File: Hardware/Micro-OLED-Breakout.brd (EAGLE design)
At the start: 27.9 x 21.6 mm, 23 parts

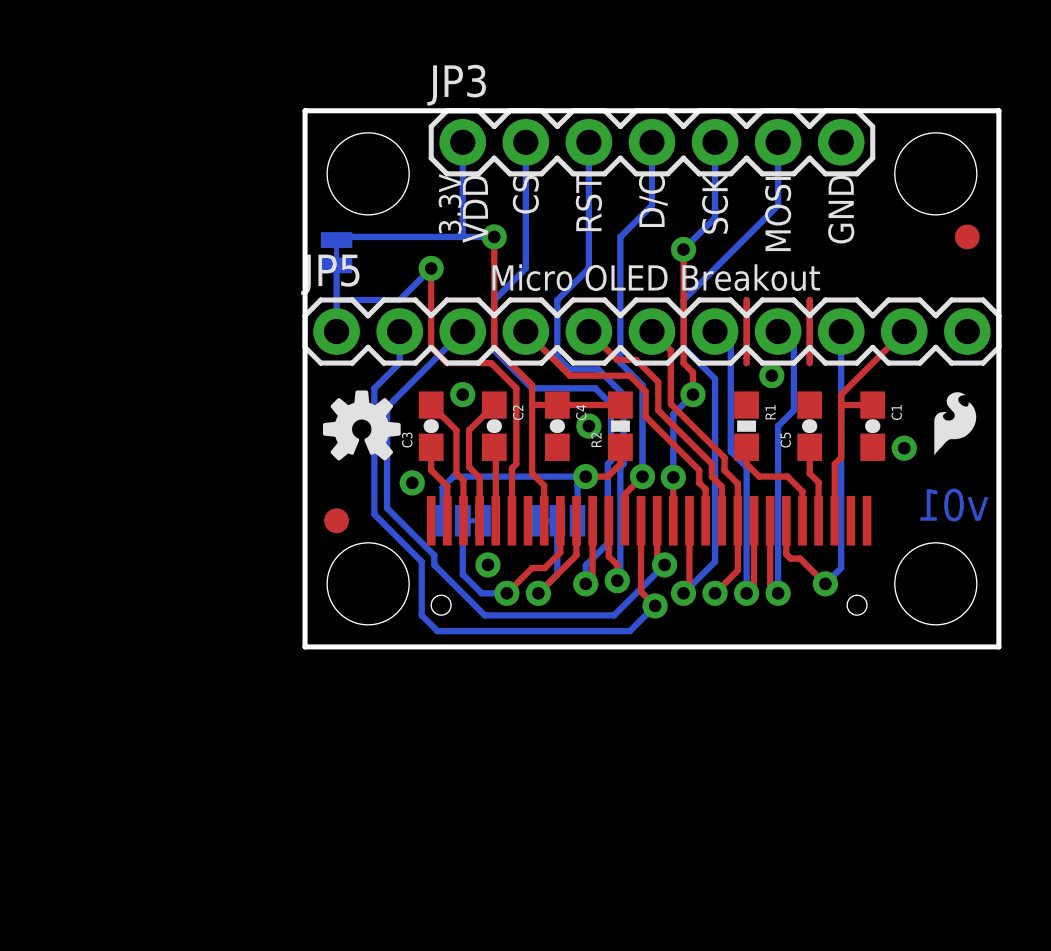
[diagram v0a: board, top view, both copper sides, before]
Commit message: Revising board shape, OLED (v02)
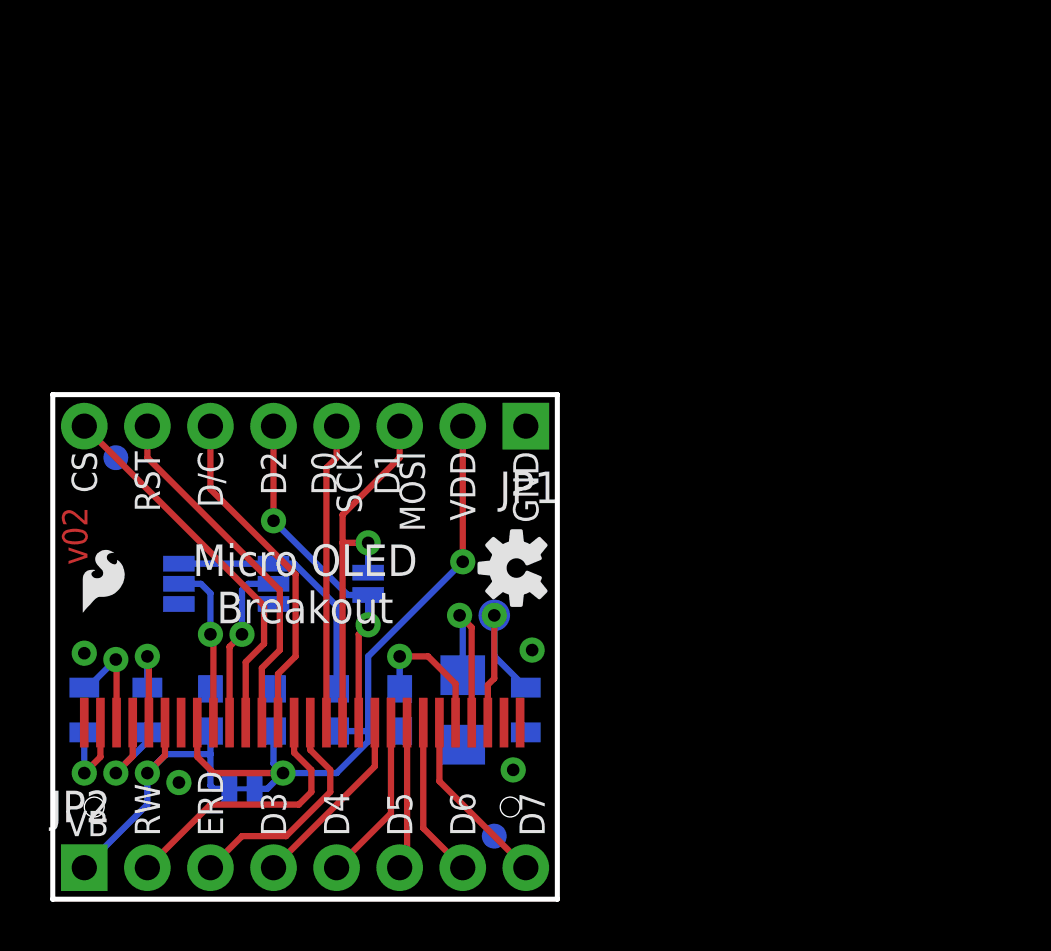
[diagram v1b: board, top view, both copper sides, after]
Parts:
- removed JP3: (no value), SparkFun-Connectors:1X07
- removed JP5: M11PTH, SparkFun-Connectors:1X11
- removed STANDOFF1, STANDOFF2, STANDOFF3, STANDOFF4: STAND-OFF, SparkFun-Electromechanical:STAND-OFF
- added C6: 1uF, SparkFun-Passives:0603-CAP
- added JP1, JP2: (no value), SparkFun-Connectors:1X08_PIN1_NO_SILK
- added LOGO4: SFE_LOGO_FLAME.1_INCH, SparkFun-Aesthetics:SFE_LOGO_FLAME_.1
- added SJ5: (no value), SparkFun-Passives:PAD-JUMPER-2-NO_YES_SILK
- added TP1: TEST-POINT3X5, SparkFun-Passives:PAD.03X.05
- C1: device SparkFun-Passives:0603-CAP -> SparkFun-Passives:0805
- C2: value 1uF 16V X5R -> 1uF X5R; device SparkFun-Passives:0603-CAP -> SparkFun-Passives:0805
- C3: value 1uF/16V X5R -> 1uF X5R; device SparkFun-Passives:0603-CAP -> SparkFun-Passives:0805
- C5: value 4.7uF/16V X7R -> 4.7uF/16V; device SparkFun-Passives:0603-CAP -> SparkFun-Passives:1206
- LOGO3: value SFE_LOGO_NAME_FLAME.1_INCH -> OSHW-LOGOS; device SparkFun-Aesthetics:SFE_LOGO_NAME_FLAME_.1 -> SparkFun-Aesthetics:OSHW-LOGO-S
- R2: value (none) -> 10k
- SJ1: value (none) -> BS1; device SparkFun-Passives:PAD-JUMPER-3-2OF3_NC_BY_TRACE_YES_SILK_FULL_BOX -> SparkFun-Passives:PAD-JUMPER-3-2OF3_NC_BY_PASTE_YES_SILK_FULL_BOX
- SJ2: value (none) -> BS2; device SparkFun-Passives:PAD-JUMPER-3-2OF3_NC_BY_TRACE_YES_SILK_FULL_BOX -> SparkFun-Passives:PAD-JUMPER-3-2OF3_NC_BY_PASTE_YES_SILK_FULL_BOX
- SJ3: device SparkFun-Passives:PAD-JUMPER-2-NC_BY_TRACE_YES_SILK -> SparkFun-Passives:PAD-JUMPER-2-NC_BY_TRACE_NO_SILK
- moved LOGO2 34.9 mm to (-9.27, 1.02)
- moved FID1 30.7 mm to (7.62, -7.62), flipped to the bottom
- moved SJ3 21.9 mm to (-2.54, -5.71), turned to 180 degrees
- moved C1 18.1 mm to (8.89, -2.54), flipped to the bottom
- moved C2 18.1 mm to (-6.35, -2.54), flipped to the bottom, turned to 90 degrees
- moved C3 18.1 mm to (-8.89, -2.54), flipped to the bottom
- moved C5 18.1 mm to (6.35, -2.54), flipped to the bottom, turned to 270 degrees
- moved R1 18.1 mm to (3.81, -2.54), flipped to the bottom, turned to 90 degrees
- moved FRAME1 16.3 mm to (-17.8, -19.1)
- moved C4 16.2 mm to (-1.27, -2.54), flipped to the bottom, turned to 90 degrees
- moved R2 16.2 mm to (1.27, -2.54), flipped to the bottom, turned to 270 degrees
- moved OLED1 16.2 mm to (-8.89, -3.05)
- moved LOGO3 11.8 mm to (8.51, 3.17), turned to 270 degrees
- moved SJ1 11.7 mm to (-1.27, 2.54), turned to 270 degrees
- moved SJ2 11.7 mm to (-5.08, 2.54), turned to 270 degrees
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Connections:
- net CS: now also JP1.8; no longer JP3.2
- net D/C: now also JP1.6; no longer JP3.4
- net D0/SCK: now also JP1.4; no longer JP3.5
- net D1/MOSI: now also JP1.3, SJ5.1; no longer JP3.6
- net D2: now also JP1.5, SJ5.2; no longer JP5.4
- net D3: now also JP2.4; no longer JP5.5
- net D4: now also JP2.5; no longer JP5.6
- net D5: now also JP2.6; no longer JP5.7
- net D6: now also JP2.7; no longer JP5.8
- net D7: now also JP2.8; no longer JP5.9
- net E/RD: now also JP2.3; no longer JP5.3
- net GND: now also C6.2, JP1.1; no longer JP3.7, JP5.11
- net R/W: now also JP2.2; no longer JP5.2
- net RESET: now also JP1.7; no longer JP3.3
- net VBAT: now also C6.1, JP2.1; no longer JP5.1
- net VCC: now also TP1.P$1; no longer JP5.10
- net VDD: now also JP1.2; no longer JP3.1
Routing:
- net R/W: track 26.4 -> 10.9 mm, vias 1 -> 0
- net E/RD: track 24.3 -> 9.22 mm, vias 1 -> 0
- net GND: track 10.2 -> 0.00 mm, vias 6 -> 4
- net CS: track 24.8 -> 15.2 mm, vias 1 -> 0
- net D1/MOSI: track 23.8 -> 15.1 mm
- net RESET: track 22.6 -> 14.4 mm, vias 1 -> 0
- net D5: track 14.1 -> 5.97 mm, vias 1 -> 0
- net D6: track 14.1 -> 6.50 mm, vias 1 -> 0
- net VBAT: track 19.7 -> 13.1 mm
- net D7: track 13.8 -> 7.28 mm, vias 1 -> 0
- net D4: track 12.4 -> 6.75 mm, vias 1 -> 0
- net D0/SCK: track 16.3 -> 12.1 mm, vias 3 -> 0
- net VCOMH: track 3.11 -> 6.98 mm, vias 0 -> 1
- net D/C: track 16.4 -> 13.7 mm, vias 1 -> 0
- net D3: track 10.3 -> 7.53 mm
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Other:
- board size 27.9 x 21.6 mm -> 20.3 x 20.3 mm
- board text added: "D0"
- board text added: "D1"
- board text added: "ERD"
- board text added: "RW"
- board text added: "VB"
- board text added: "VD/VB"
- board text added: "v02"
- board text removed: "3.3V"
- board text removed: "7V"
- board text removed: "E/RD"
- board text removed: "R/W"
- board text removed: "VBAT"
- board text removed: "VCC"
- board text removed: "v01"

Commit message: Fixing swapped BS1 and BS2 labels (v03)
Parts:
- added TP2: TEST-POINT3X5, SparkFun-Passives:PAD.03X.05
- moved SJ1 3.81 mm to (-5.08, 2.54)
- moved SJ2 3.81 mm to (-1.27, 2.54)
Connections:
- net BS1: now also OLED1.9; no longer OLED1.10
- net BS2: now also OLED1.10; no longer OLED1.9
- net VCC: now also TP2.P$1
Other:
- board text added: "v03"
- board text removed: "v02"
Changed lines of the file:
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@@
 <layer number="47" name="Measures" color="7" fill="1" visible="no" active="yes"/>
 <layer number="48" name="Document" color="7" fill="1" visible="no" active="yes"/>
-<layer number="49" name="Reference" color="7" fill="1" visible="no" active="yes"/>
+<layer number="49" name="Reference" color="7" fill="1" visible="yes" active="yes"/>
 <layer number="50" name="dxf" color="7" fill="1" visible="no" active="no"/>
 <layer number="51" name="tDocu" color="6" fill="1" visible="yes" active="yes"/>
@@
 <wire x1="10.16" y1="10.16" x2="10.16" y2="-10.16" width="0.2032" layer="20"/>
 <wire x1="10.16" y1="-10.16" x2="-10.16" y2="-10.16" width="0.2032" layer="20"/>
-<text x="-5.334" y="0.381" size="0.889" layer="22" font="vector" ratio="15" rot="MR180" align="center">BS2</text>
-<text x="-1.397" y="0.381" size="0.889" layer="22" font="vector" ratio="15" rot="MR0" align="center">BS1</text>
+<text x="-5.334" y="0.381" size="0.889" layer="22" font="vector" ratio="15" rot="MR180" align="center">BS1</text>
+<text x="-1.397" y="0.381" size="0.889" layer="22" font="vector" ratio="15" rot="MR0" align="center">BS2</text>
 <text x="-3.302" y="1.651" size="0.889" layer="22" font="vector" ratio="15" rot="MR0" align="center">0</text>
 <text x="-3.302" y="3.302" size="0.889" layer="22" font="vector" ratio="15" rot="MR0" align="center">1</text>
 <text x="8.89" y="-19.05" size="1.778" layer="51" ratio="15">Jim Lindblom</text>
-<text x="-8.763" y="3.302" size="1.016" layer="1" font="vector" ratio="15" rot="R90">v02</text>
+<text x="-8.763" y="3.302" size="1.016" layer="1" font="vector" ratio="15" rot="R90">v03</text>
 <text x="3.556" y="3.048" size="0.889" layer="22" font="vector" ratio="15" rot="MR0" align="center-right">D1</text>
 <text x="3.556" y="2.032" size="0.889" layer="22" font="vector" ratio="15" rot="MR0" align="center-right">D2</text>
@@
 <wire x1="-4.064" y1="3.302" x2="-3.683" y2="3.302" width="0.1778" layer="22"/>
 <wire x1="-4.064" y1="1.651" x2="-3.683" y2="1.651" width="0.1778" layer="22"/>
+<wire x1="-2.159" y1="-5.715" x2="-2.921" y2="-5.715" width="0.254" layer="30"/>
 </plain>
 <attributes>
@@
 <element name="TP1" library="SparkFun-Passives" package="PAD.03X.05" value="TEST-POINT3X5" x="7.62" y="1.27" rot="MR0"/>
 <element name="C6" library="SparkFun-Passives" package="0603-CAP" value="1uF" x="-3.81" y="-2.54" rot="MR90"/>
-<element name="SJ1" library="SparkFun-Passives" package="PAD-JUMPER-3-2OF3_NC_BY_PASTE_YES_SILK_FULL_BOX" value="BS1" x="-1.27" y="2.54" rot="MR270"/>
-<element name="SJ2" library="SparkFun-Passives" package="PAD-JUMPER-3-2OF3_NC_BY_PASTE_YES_SILK_FULL_BOX" value="BS2" x="-5.08" y="2.54" rot="MR270"/>
+<element name="SJ1" library="SparkFun-Passives" package="PAD-JUMPER-3-2OF3_NC_BY_PASTE_YES_SILK_FULL_BOX" value="BS1" x="-5.08" y="2.54" rot="MR270"/>
+<element name="SJ2" library="SparkFun-Passives" package="PAD-JUMPER-3-2OF3_NC_BY_PASTE_YES_SILK_FULL_BOX" value="BS2" x="-1.27" y="2.54" rot="MR270"/>
 <element name="LOGO3" library="SparkFun-Aesthetics" package="OSHW-LOGO-S" value="OSHW-LOGOS" x="8.509" y="3.175" rot="MR270"/>
 <element name="LOGO4" library="SparkFun-Aesthetics" package="SFE_LOGO_FLAME_.1" value="SFE_LOGO_FLAME.1_INCH" x="-6.985" y="1.016" rot="MR0"/>
+<element name="TP2" library="SparkFun-Passives" package="PAD.03X.05" value="TEST-POINT3X5" x="7.62" y="1.27"/>
 </elements>
 <signals>
@@
 </signal>
 <signal name="BS1">
+<contactref element="SJ1" pad="2"/>
+<contactref element="OLED1" pad="9"/>
+<wire x1="-3.69" y1="-3.048" x2="-3.69" y2="0.388" width="0.254" layer="1"/>
+<wire x1="-3.69" y1="0.388" x2="-3.81" y2="0.508" width="0.254" layer="1"/>
+<via x="-3.81" y="0.508" extent="1-16" drill="0.508"/>
+<wire x1="-4.191" y1="2.54" x2="-3.81" y2="2.159" width="0.254" layer="16"/>
+<wire x1="-3.81" y1="2.159" x2="-3.81" y2="0.508" width="0.254" layer="16"/>
+<wire x1="-5.08" y1="2.54" x2="-4.191" y2="2.54" width="0.254" layer="16"/>
+</signal>
+<signal name="BS2">
+<contactref element="SJ2" pad="2"/>
 <contactref element="OLED1" pad="10"/>
 <wire x1="-3.04" y1="-3.048" x2="-3.04" y2="0.008" width="0.254" layer="1"/>
@@
 <wire x1="-2.54" y1="2.286" x2="-2.286" y2="2.54" width="0.254" layer="16"/>
 <wire x1="-2.54" y1="0.508" x2="-2.54" y2="2.286" width="0.254" layer="16"/>
-<contactref element="SJ1" pad="2"/>
 <wire x1="-2.286" y1="2.54" x2="-1.27" y2="2.54" width="0.254" layer="16"/>
-</signal>
-<signal name="BS2">
-<contactref element="OLED1" pad="9"/>
-<wire x1="-3.69" y1="-3.048" x2="-3.69" y2="0.388" width="0.254" layer="1"/>
-<wire x1="-3.69" y1="0.388" x2="-3.81" y2="0.508" width="0.254" layer="1"/>
-<via x="-3.81" y="0.508" extent="1-16" drill="0.508"/>
-<wire x1="-4.191" y1="2.54" x2="-3.81" y2="2.159" width="0.254" layer="16"/>
-<wire x1="-3.81" y1="2.159" x2="-3.81" y2="0.508" width="0.254" layer="16"/>
-<contactref element="SJ2" pad="2"/>
-<wire x1="-4.191" y1="2.54" x2="-5.08" y2="2.54" width="0.254" layer="16"/>
 </signal>
 <signal name="VDD">
@@
 <wire x1="8.89" y1="-1.64" x2="7.62" y2="-0.37" width="0.254" layer="16"/>
 <wire x1="7.62" y1="-0.37" x2="7.62" y2="1.27" width="0.254" layer="16"/>
+<contactref element="TP2" pad="P$1"/>
 </signal>
 <signal name="VDD_PU">
@@
 <contactref element="SJ1" pad="1"/>
 <contactref element="SJ2" pad="1"/>
-<wire x1="-5.08" y1="3.3528" x2="-1.27" y2="3.3528" width="0.254" layer="16"/>
 <wire x1="-0.4318" y1="3.3528" x2="-1.27" y2="3.3528" width="0.254" layer="16"/>
+<wire x1="-1.27" y1="3.3528" x2="-5.08" y2="3.3528" width="0.254" layer="16"/>
 </signal>
 </signals>

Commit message: Adding D/C jumper (open by default) (v04)
Allows address selection in I2C mode.

Also:
* adding some notes to schematic
* Shuffling around silk labels. Avoiding holes.
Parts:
- removed LOGO1: OSHW-LOGOS, SparkFun-Aesthetics:OSHW-LOGO-S
- added SJ4: (no value), SparkFun-Passives:PAD-JUMPER-3-NO-TIGHT
- moved LOGO4 16.4 mm to (9.40, 1.40)
- moved SJ1 3.81 mm to (-8.89, 2.54)
- moved SJ2 3.81 mm to (-5.08, 2.54)
- moved FID1 1.80 mm to (6.35, -6.35)
- moved FID2 1.80 mm to (-8.89, 6.35)
- moved LOGO2 1.25 mm to (-8.76, 2.16)
- moved LOGO3 0.59 mm to (8.13, 3.62), flipped to the top, turned to 0 degrees
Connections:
- net E/RD renamed RD/E
- net R/W renamed WR/RW
- net D/C: now also SJ4.2
- net GND: now also SJ4.3
- net VDD_PU: now also SJ4.1
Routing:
- net D/C: track 13.7 -> 18.1 mm, vias 0 -> 1
- net VDD_PU: track 10.4 -> 14.2 mm
- net BS1: track 6.68 -> 8.78 mm
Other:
- board text added: "3V3"
- board text added: "E"
- board text added: "R/W"
- board text added: "RD"
- board text added: "SDI"
- board text added: "SDO"
- board text added: "WR"
- board text added: "v04"
- board text removed: "ERD"
- board text removed: "MOSI"
- board text removed: "RW"
- board text removed: "v03"

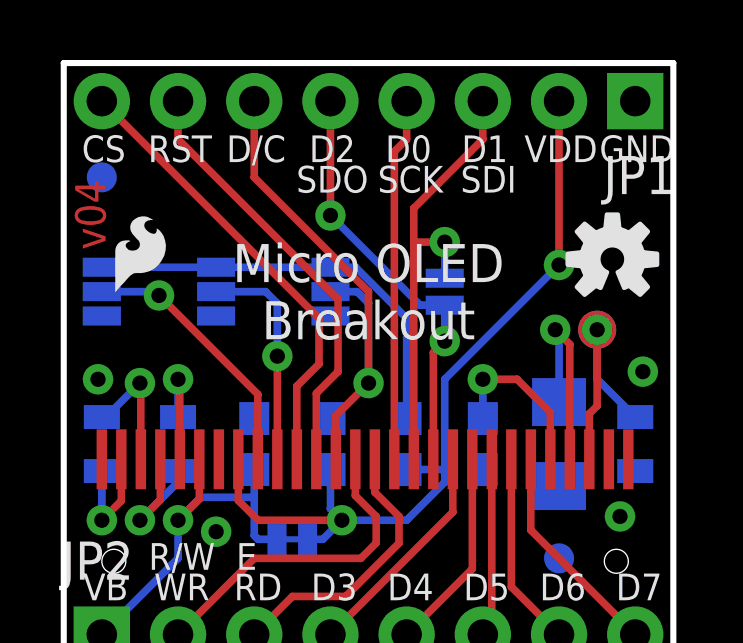
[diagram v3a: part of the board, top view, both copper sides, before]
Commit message: Couple minor silk, via placement adjustments (v04)
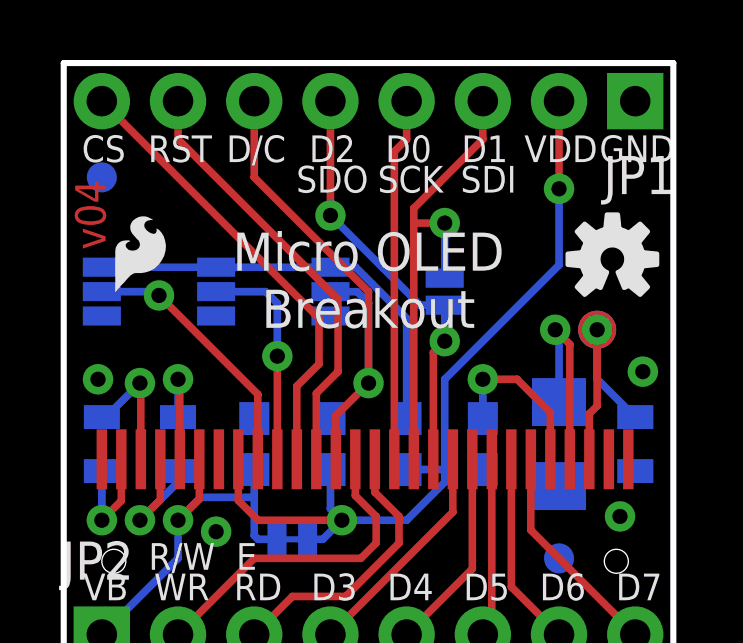
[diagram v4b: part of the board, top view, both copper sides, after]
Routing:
- net D1/MOSI: track 15.1 -> 15.8 mm
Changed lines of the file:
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@@
 <text x="3.8735" y="7.747" size="0.889" layer="21" font="vector" ratio="15" align="top-center">D1</text>
 <text x="4.0005" y="6.731" size="0.889" layer="21" font="vector" ratio="15" align="top-center">SDI</text>
-<text x="0" y="2.54" size="1.27" layer="21" font="vector" ratio="15" align="center">Micro OLED
+<text x="0" y="2.921" size="1.27" layer="21" font="vector" ratio="15" align="center">Micro OLED
 Breakout</text>
 <text x="-8.763" y="-7.747" size="0.889" layer="21" font="vector" ratio="15" align="bottom-center">VB</text>
@@
 <wire x1="2.54" y1="-3.81" x2="2.54" y2="-3.429" width="0.254" layer="16"/>
 <wire x1="2.54" y1="-3.429" x2="2.54" y2="-0.381" width="0.254" layer="16"/>
-<wire x1="2.54" y1="-0.381" x2="6.35" y2="3.429" width="0.254" layer="16"/>
-<wire x1="6.35" y1="8.89" x2="6.35" y2="3.429" width="0.254" layer="1"/>
-<via x="6.35" y="3.429" extent="1-16" drill="0.508"/>
+<wire x1="6.35" y1="8.89" x2="6.35" y2="5.969" width="0.254" layer="1"/>
+<via x="6.35" y="5.969" extent="1-16" drill="0.508"/>
 <via x="-0.889" y="-5.08" extent="1-16" drill="0.508"/>
 <wire x1="-0.889" y1="-5.08" x2="-3.683" y2="-5.08" width="0.254" layer="1"/>
@@
 <wire x1="-2.032" y1="-5.715" x2="-1.524" y2="-5.715" width="0.254" layer="16"/>
 <wire x1="-1.524" y1="-5.715" x2="-0.889" y2="-5.08" width="0.254" layer="16"/>
+<wire x1="2.54" y1="-0.381" x2="6.35" y2="3.429" width="0.254" layer="16"/>
+<wire x1="6.35" y1="3.429" x2="6.35" y2="5.969" width="0.254" layer="16"/>
 </signal>
 <signal name="VCOMH">
@@
 <contactref element="SJ5" pad="1"/>
 <contactref element="JP1" pad="3"/>
-<wire x1="1.51" y1="-3.048" x2="1.51" y2="4.191" width="0.254" layer="1"/>
-<wire x1="1.51" y1="4.191" x2="1.51" y2="5.32" width="0.254" layer="1"/>
+<wire x1="1.51" y1="-3.048" x2="1.51" y2="4.826" width="0.254" layer="1"/>
+<wire x1="1.51" y1="4.826" x2="1.51" y2="5.32" width="0.254" layer="1"/>
 <wire x1="1.51" y1="5.32" x2="3.81" y2="7.62" width="0.254" layer="1"/>
 <wire x1="3.81" y1="7.62" x2="3.81" y2="8.89" width="0.254" layer="1"/>
-<wire x1="2.54" y1="2.99" x2="2.54" y2="4.191" width="0.254" layer="16"/>
-<via x="2.54" y="4.191" extent="1-16" drill="0.508"/>
-<wire x1="2.54" y1="4.191" x2="1.51" y2="4.191" width="0.254" layer="1"/>
+<wire x1="2.54" y1="2.99" x2="2.54" y2="4.826" width="0.254" layer="16"/>
+<via x="2.54" y="4.826" extent="1-16" drill="0.508"/>
+<wire x1="2.54" y1="4.826" x2="1.51" y2="4.826" width="0.254" layer="1"/>
 </signal>
 <signal name="D0/SCK">
